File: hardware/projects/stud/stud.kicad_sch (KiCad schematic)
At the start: 6 parts, among them IC1 R7KA8M2JFLCAC#UC0, IC2 IS42S32160F-7BLI, U1 TPS629210DRLR, U2 TAC5242, Y1 X1G0044510004

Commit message: label other signal lines
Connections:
- net EXTAL: now reaches Y1.3 (OUT)
- net EXTAL: now also IC1.K17 (P212/E_XTAL)
- net μSD_DAT2: now reaches MICRO_SD1.1 (DAT2)
- net μSD_DAT2: now also IC1.B16 (PD01)
- net μSD_DAT3: now reaches MICRO_SD1.2 (CD/DAT3)
- net μSD_DAT3: now also IC1.E8 (P111)
- net μSD_CMD: now reaches MICRO_SD1.3 (CMD)
- net μSD_CMD: now also IC1.C14 (PD04)
- net μSD_CLK: now reaches MICRO_SD1.5 (CLK)
- net μSD_CLK: now also IC1.C16 (PD05)
- net μSD_DAT0: now reaches MICRO_SD1.7 (DAT0)
- net μSD_DAT0: now also IC1.C15 (PD03)
- net μSD_DAT1: now reaches MICRO_SD1.8 (DAT1)
- net μSD_DAT1: now also IC1.B17 (PD02)
- net μSD_CD: now reaches MICRO_SD1.CD1 (CD)
- net μSD_CD: now also IC1.D11 (P306)
- net SSI_RX: now reaches IC1.F14 (P406)
- net SSI_RX: now also U2.4 (DOUT)
- net SSI_TX: now reaches IC1.G12 (P405)
- net SSI_TX: now also U2.5 (DIN)
- net SSI_BCK: now reaches IC1.H13 (P403)
- net SSI_BCK: now also U2.2 (BCLK)
- net SSI_FS: now reaches IC1.J13 (P404)
- net SSI_FS: now also U2.3 (FSYNC)
- no-connect marks 0 -> 6
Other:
- note added: "GPO latched high ⇒ clock error; have to power-cycle to clear, but good debug item?"
- note added: "MICBIAS is an output to bias mics; bring out to test point?"
- note added: "pin groups: - SSI*0_A for audio - SD0*_C for μSD"
- moved on the sheet: Y1

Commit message: hook up all chips except the 3.3 V buck
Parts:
- added C1, C10, C11, C12, C13, C14, C15, C17, C2, C3, C31, C32, C33, C34, C35, C36, C37, C38, C39, C4, C40, C41, C42, C43, C44, C45, C48, C5, C50, C52, C6, C7, C8, C9: 100n, symbol Device:C
- added C16, C46, C47, C49, C53, C54, C55: 22u, symbol Device:C
- added C18, C19, C20, C21, C22, C23, C24, C25, C26, C27, C28, C29: 220n, symbol Device:C
- added C30: 47u, symbol Device:C
- added C51: 1u, symbol Device:C
- added C58, C59: 2.2u, symbol Device:C
- added JP1: SolderJumper_2_Bridged, symbol Jumper:SolderJumper_2_Bridged
- added L1: 2.2u, symbol Device:L
- added R1: 5.1, symbol Device:R_US
- added R2, R3: 100k, symbol Device:R_US
- added TP1, TP2: TestPoint, symbol Connector:TestPoint
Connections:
- net SHIELD is gone; now on net GND: MICRO_SD1.MP2 (SHIELD), MICRO_SD1.MP3 (SHIELD), MICRO_SD1.MP4 (SHIELD)
- net +3V3: now reaches Y1.1 (~{ST})
- net +3V3: now also IC1.A10 (VCC_DCDC_1), IC1.A11 (VCC_DCDC_2), IC1.B10 (VCC_DCDC_3), IC1.B11 (VCC_DCDC_4), IC1.F11 (VCC_07), IC1.F6 (VCC_08), IC1.G11 (VCC_06), IC1.G16 (VCC_05), IC1.G6 (VCC_09), IC1.H11 (VCC_04), IC1.H14 (VCC_03), IC1.H6 (VCC_10), IC1.J6 (VCC2_11), IC1.K14 (VCC_02), IC1.L15 (VCC_01), IC1.L6 (VCC2_12), IC1.M7 (VCC2_14), IC1.M8 (VCC2_15), IC1.R1 (VCC2_13), IC2.A7 (VDD_1), IC2.B2 (VDDQ_1), IC2.B7 (VDDQ_2), IC2.C9 (VDDQ_3), IC2.D9 (VDDQ_4), IC2.E1 (VDDQ_5), IC2.F9 (VDD_2), IC2.L1 (VDDQ_6), IC2.L7 (VDD_3), IC2.M9 (VDDQ_7), IC2.N9 (VDDQ_8), IC2.P2 (VDDQ_9), IC2.P7 (VDDQ_10), IC2.R7 (VDD_4), MICRO_SD1.4 (VDD), U2.12 (MD5), U2.6 (IOVDD), Y1.4 (VCC), C1.1, C10.1, C11.1, C12.1, C13.1, C14.1, C15.1, C16.1, C17.1, C2.1, C3.1, C31.1, C32.1, C33.1, C34.1, C35.1, C36.1, C37.1, C38.1, C39.1, C4.1, C40.1, C41.1, C42.1, C43.1, C44.1, C45.2, C5.1, C52.1, C6.1, C7.1, C8.1, C9.1, R1.1
- net GND: now reaches Y1.2 (GND)
- net GND: now also IC1.A9 (VSS_DCDC_1), IC1.B9 (VSS_DCDC_2), IC1.F10 (VSS_07), IC1.F7 (VSS_08), IC1.F8 (VSS3), IC1.G10 (VSS_06), IC1.G15 (VSS_03), IC1.G17 (VSS_05), IC1.G7 (VSS_09), IC1.G8 (VSS4), IC1.H10 (VSS5), IC1.H7 (VSS_10), IC1.H8 (VSS7), IC1.J10 (VSS6), IC1.J12 (VSS2), IC1.J14 (VSS_02), IC1.J7 (VSS_11), IC1.K10 (VSS8), IC1.K12 (VSS1), IC1.K6 (VSS_12), IC1.K7 (VSS9), IC1.L12 (VSS0), IC1.L7 (VSS_14), IC1.L8 (VSS_15), IC1.L9 (VSS10), IC1.M10 (VSS11), IC1.M17 (VSS_01), IC1.U4 (VSS_13), IC2.A3 (VSS_1), IC2.B3 (VSSQ_1), IC2.B8 (VSSQ_2), IC2.C1 (VSSQ_3), IC2.D1 (VSSQ_4), IC2.E9 (VSSQ_5), IC2.F1 (VSS_2), IC2.L3 (VSS_3), IC2.L9 (VSSQ_6), IC2.M1 (VSSQ_7), IC2.N1 (VSSQ_8), IC2.P3 (VSSQ_9), IC2.P8 (VSSQ_10), IC2.R3 (VSS_4), MICRO_SD1.6 (VSS), MICRO_SD1.MP1 (SHIELD), U2.10 (MD4), U2.13 (MD0), U2.7 (MD1), U2.8 (MD2), U2.9 (MD3), C1.2, C10.2, C11.2, C12.2, C13.2, C14.2, C15.2, C16.2, C17.2, C18.2, C19.2, C2.2, C20.2, C21.2, C22.2, C23.2, C24.2, C25.2, C26.2, C27.2, C28.2, C29.2, C3.2, C30.2, C31.2, C32.2, C33.2, C34.2, C35.2, C36.2, C37.2, C38.2, C39.2, C4.2, C40.2, C41.2, C42.2, C43.2, C44.2, C45.1, C49.2, C5.2, C50.2, C52.2, C6.2, C7.2, C8.2, C9.2, JP1.2 (B)
- net VLO: now reaches IC1.A7 (VLO_1)
- net VLO: now also IC1.A8 (VLO_2), IC1.B7 (VLO_3), IC1.B8 (VLO_4), L1.1
- net +0V9: now reaches IC1.G9 (VCL4)
- net +0V9: now also IC1.H9 (VCL5), IC1.J8 (VCL7), IC1.J9 (VCL6), IC1.K11 (VCL1), IC1.K8 (VCL9), IC1.K9 (VCL8), IC1.L11 (VCL0), IC1.M11 (VCL11), C18.1, C19.1, C20.1, C21.1, C22.1, C23.1, C24.1, C25.1, C26.1, C27.1, C28.1, C29.1, C30.1, L1.2
- net at U2.1 (DREG): now also C49.1, C50.1
- net CODEC_ERROR: now reaches U2.11 (GPO)
- net CODEC_ERROR: now also TP2.1
- net at U2.14 (MICBIAS): now also TP1.1
- net at U2.15 (IN1P): now also C47.2
- net at U2.16 (IN1M): now also C53.2
- net at U2.17 (IN2P): now also C54.2
- net at U2.18 (IN2M): now also C55.2
- net at U2.20 (OUT1P): now also C58.1
- net at U2.21 (OUT2P): now also C59.1
- net +3V3A: now reaches U2.23 (AVDD)
- net +3V3A: now also C46.1, C48.1, R1.2
- net at U2.24 (VREF): now also C51.1
- net GNDA: now reaches U2.A1 (VSS)
- net GNDA: now also U2.A2 (VSS), U2.A3 (VSS), U2.A4 (VSS), U2.TP (VSS), C46.2, C48.2, C51.2, C53.1, C55.1, JP1.1 (A), R2.2, R3.2
- new net IN_L: C47.1
- new net IN_R: C54.1
- new net OUT_L: C58.2, R3.1
- new net OUT_R: C59.2, R2.1
- no-connect marks 6 -> 8
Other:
- note added: "VLO buck output"
- note added: "bypass caps for VCC_01 to VCC2_15"
- note added: "bypass caps for VCC_DCDC"
- note added: "bypass caps for VCL0 to VLC11"
- note added: "bypass caps for VDD/VDDQ"
- note added: "configured for - target I2S - AVDD = 3V3, 32-bit word, linear-phase - input HPF cutoff @ 1 Hz - single-ended I/O, AC-coupled"
- moved on the sheet: IC2, MICRO_SD1, U1, U2, Y1

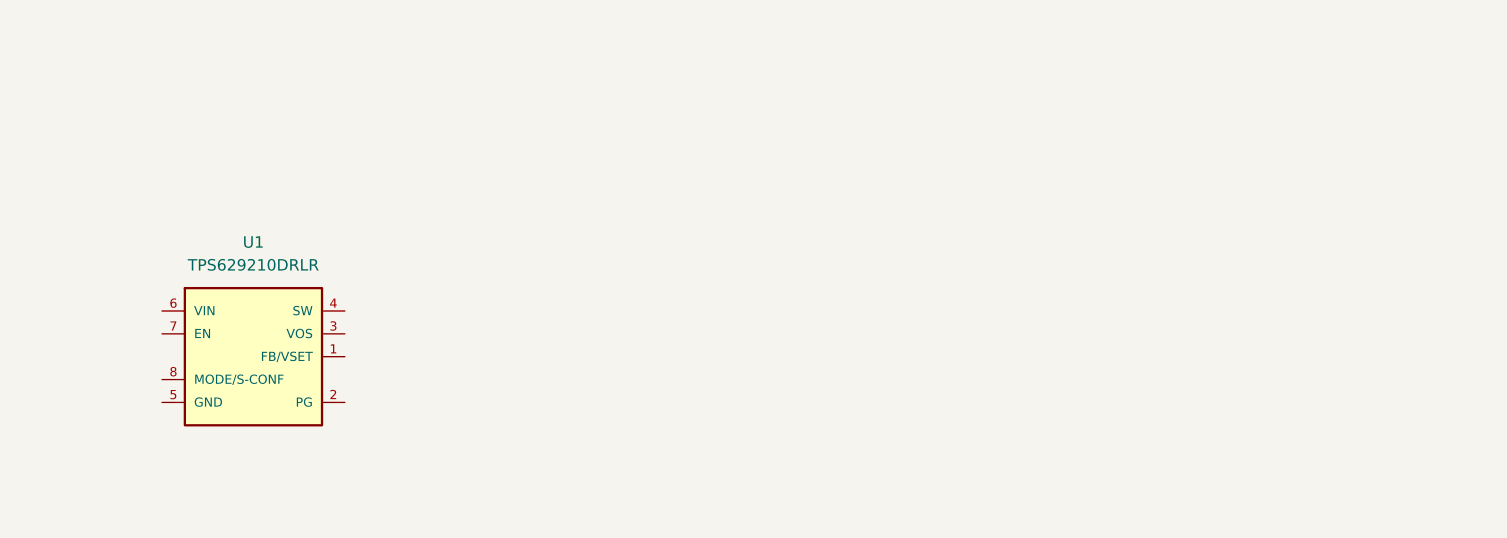
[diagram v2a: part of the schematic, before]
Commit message: set up buck converter
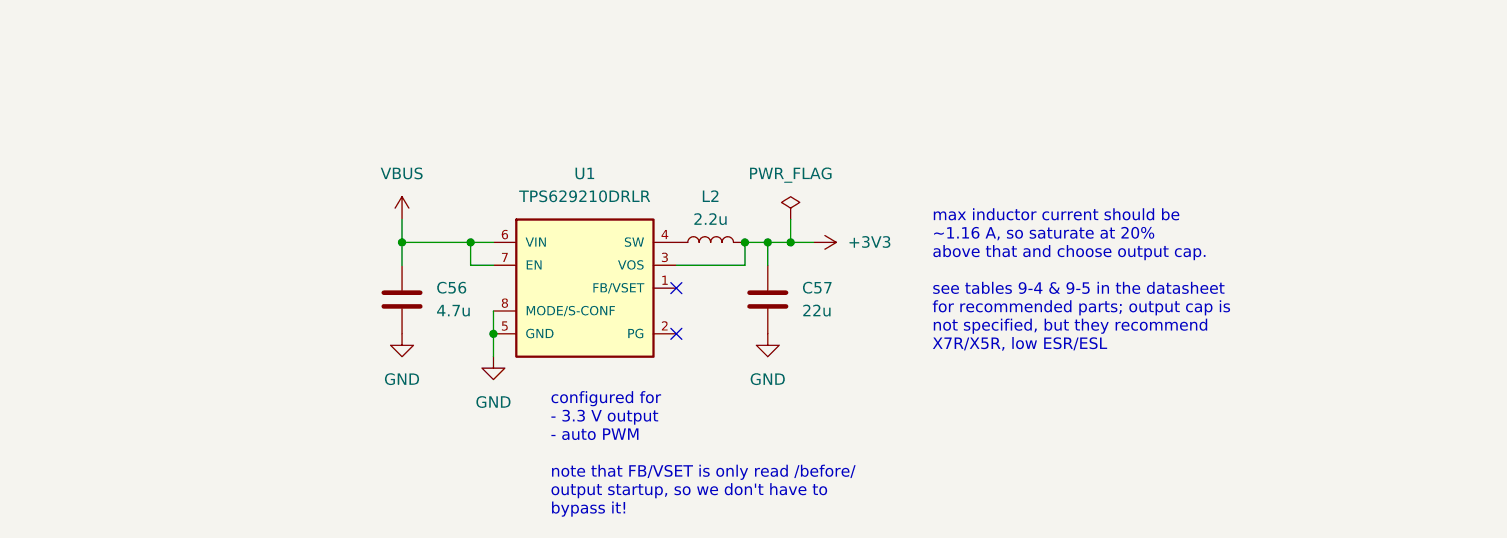
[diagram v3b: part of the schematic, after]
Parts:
- added C56: 4.7u, symbol Device:C
- added C57: 22u, symbol Device:C
- added L2: 2.2u, symbol Device:L
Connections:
- net +3V3: now also U1.3 (VOS), C57.1, L2.2
- net GND: now also U1.5 (GND), U1.8 (MODE/S-CONF), C56.2, C57.2
- net at U1.4 (SW): now also L2.1
- net VBUS: now reaches U1.6 (VIN)
- net VBUS: now also U1.7 (EN), C56.1
- no-connect marks 8 -> 10
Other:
- note added: "configured for - 3.3 V output - auto PWM note that FB/VSET is only read /before/ output startup, so we don't have to bypass it!"
- note added: "max inductor current should be ~1.16 A, so saturate at 20% above that and choose output cap. see tables 9-4 & 9-5 in the datasheet for recommended parts; output cap is not specified, but they recommend X7R/X5R, low ESR/ESL"
- moved on the sheet: U1

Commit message: add a USB port
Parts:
- added D1, D2: D, symbol Device:D
- added J1: USB_C_Receptacle_USB2.0_16P, Connector_USB:USB_C_Receptacle_G-Switch_GT-USB-7010ASV, symbol Connector:USB_C_Receptacle_USB2.0_16P
- added R4: 2.20k 1%, symbol Device:R_US
- added R5, R6: 5.1k, symbol Device:R_US
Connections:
- net +3V3: now also IC1.H15 (VCC_USBHS), IC1.K15 (AVCC_USBHS), IC1.U17 (VCC_USB)
- net GND: now also IC1.H12 (VSS_04), IC1.J16 (VSS2_USBHS), IC1.J17 (VSS1_USBHS), IC1.T17 (VSS_USB), J1.A1 (GND), J1.A12 (GND), J1.B1 (GND), J1.B12 (GND), J1.SH (SHIELD), R4.2, R5.2, R6.2
- net VBUS: now also IC1.M15 (P408), D1.2 (A), J1.A4 (VBUS), J1.A9 (VBUS), J1.B4 (VBUS), J1.B9 (VBUS); no longer C56.1, U1.6 (VIN), U1.7 (EN)
- net USB_D+: now reaches IC1.H16 (USBHS_DP)
- net USB_D+: now also J1.A6 (D+), J1.B6 (D+)
- net USB_D-: now reaches IC1.H17 (USBHS_DM)
- net USB_D-: now also J1.A7 (D-), J1.B7 (D-)
- net at IC1.J15 (USBHS_RREF): now also R4.1
- new net: J1.B5 (CC2), R6.1
- new net: J1.A5 (CC1), R5.1
- new net +9V: D2.2 (A)
- new net VDC: C56.1, D1.1 (K), D2.1 (K), U1.6 (VIN), U1.7 (EN)
- no-connect marks 10 -> 12

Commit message: decide on a few IO pins
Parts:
- added J2: DAC0, custom:Connector_01x01_CastellatedEdge, symbol custom:Connector_01x01_CastellatedEdge
- added J3: ADC1_8, custom:Connector_01x01_CastellatedEdge, symbol custom:Connector_01x01_CastellatedEdge
- added J4: DAC1, custom:Connector_01x01_CastellatedEdge, symbol custom:Connector_01x01_CastellatedEdge
- added J5: ADC1_6, custom:Connector_01x01_CastellatedEdge, symbol custom:Connector_01x01_CastellatedEdge
- added J6: ADC1_0, custom:Connector_01x01_CastellatedEdge, symbol custom:Connector_01x01_CastellatedEdge
- added J7: ADC1_2, custom:Connector_01x01_CastellatedEdge, symbol custom:Connector_01x01_CastellatedEdge
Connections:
- net at IC1.T8 (P014): now also J2.1
- net at IC1.U11 (P008): now also J3.1
- net at IC1.U12 (P006): now also J5.1
- net at IC1.U13 (P000): now also J6.1
- net at IC1.U14 (P002): now also J7.1
- net at IC1.U8 (P015): now also J4.1

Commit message: choose two I2C interfaces
that might be too many, given that there's a more configurable
peripheral interface. maybe only one hardware I2C and the rest are
"simple?"
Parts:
- added J10: SCL1_A, custom:Connector_01x01_CastellatedEdge, symbol custom:Connector_01x01_CastellatedEdge
- added J11: SDA1_A, custom:Connector_01x01_CastellatedEdge, symbol custom:Connector_01x01_CastellatedEdge
- added J8: SCL0_A, custom:Connector_01x01_CastellatedEdge, symbol custom:Connector_01x01_CastellatedEdge
- added J9: SDA0_A, custom:Connector_01x01_CastellatedEdge, symbol custom:Connector_01x01_CastellatedEdge
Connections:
- net at IC1.K13 (P410): now also J8.1
- net at IC1.P13 (P512): now also J10.1
- net at IC1.R16 (P409): now also J9.1
- net at IC1.U15 (P511): now also J11.1

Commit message: talk to claude about SDRAM and GPIOs
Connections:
- net +0V9: now also IC1.F9 (VCL3), IC1.J11 (VCL2), IC1.L10 (VCL10)
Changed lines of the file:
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@@
 	)
 	(symbol
+		(lib_id "custom:+0V9")
+		(at 107.95 180.34 270)
+		(unit 1)
+		(body_style 1)
+		(exclude_from_sim no)
+		(in_bom yes)
+		(on_board yes)
+		(in_pos_files yes)
+		(dnp no)
+		(fields_autoplaced yes)
+		(property "Reference" "#PWR0140"
+			(at 104.14 180.34 0)
+			(hide yes)
+			(show_name no)
+			(do_not_autoplace no)
+			(effects
+				(font
+					(size 1.27 1.27)
+				)
+			)
+		)
+		(property "Value" "+0V9"
+			(at 111.76 180.3399 90)
+			(show_name no)
+			(do_not_autoplace no)
+			(effects
+				(font
+					(size 1.27 1.27)
+				)
+				(justify left)
+			)
+		)
+		(property "Footprint" ""
+			(at 107.95 180.34 0)
+			(hide yes)
+			(show_name no)
+			(do_not_autoplace no)
+			(effects
+				(font
+					(size 1.27 1.27)
+				)
+			)
+		)
+		(property "Datasheet" ""
+			(at 107.95 180.34 0)
+			(hide yes)
+			(show_name no)
+			(do_not_autoplace no)
+			(effects
+				(font
+					(size 1.27 1.27)
+				)
+			)
+		)
+		(property "Description" "Power symbol creates a global label with name \"+0V9\""
+			(at 107.95 180.34 0)
+			(hide yes)
+			(show_name no)
+			(do_not_autoplace no)
+			(effects
+				(font
+					(size 1.27 1.27)
+				)
+			)
+		)
+		(pin "1"
+		)
+		(instances
+			(project "stud"
+				(path "/5a440a9e-b660-4605-bd2b-6a991cc5b149"
+					(reference "#PWR0140")
+					(unit 1)
+				)
+			)
+		)
+	)
+	(symbol
 		(lib_id "Device:R_US")
 		(at 326.39 402.59 0)
@@
 	)
 	(symbol
+		(lib_id "custom:+0V9")
+		(at 46.99 330.2 90)
+		(unit 1)
+		(body_style 1)
+		(exclude_from_sim no)
+		(in_bom yes)
+		(on_board yes)
+		(in_pos_files yes)
+		(dnp no)
+		(fields_autoplaced yes)
+		(property "Reference" "#PWR0139"
+			(at 50.8 330.2 0)
+			(hide yes)
+			(show_name no)
+			(do_not_autoplace no)
+			(effects
+				(font
+					(size 1.27 1.27)
+				)
+			)
+		)
+		(property "Value" "+0V9"
+			(at 43.18 330.1999 90)
+			(show_name no)
+			(do_not_autoplace no)
+			(effects
+				(font
+					(size 1.27 1.27)
+				)
+				(justify left)
+			)
+		)
+		(property "Footprint" ""
+			(at 46.99 330.2 0)
+			(hide yes)
+			(show_name no)
+			(do_not_autoplace no)
+			(effects
+				(font
+					(size 1.27 1.27)
+				)
+			)
+		)
+		(property "Datasheet" ""
+			(at 46.99 330.2 0)
+			(hide yes)
+			(show_name no)
+			(do_not_autoplace no)
+			(effects
+				(font
+					(size 1.27 1.27)
+				)
+			)
+		)
+		(property "Description" "Power symbol creates a global label with name \"+0V9\""
+			(at 46.99 330.2 0)
+			(hide yes)
+			(show_name no)
+			(do_not_autoplace no)
+			(effects
+				(font
+					(size 1.27 1.27)
+				)
+			)
+		)
+		(pin "1"
+		)
+		(instances
+			(project "stud"
+				(path "/5a440a9e-b660-4605-bd2b-6a991cc5b149"
+					(reference "#PWR0139")
+					(unit 1)
+				)
+			)
+		)
+	)
+	(symbol
 		(lib_id "power:GND")
 		(at 107.95 241.3 90)
@@
 					(unit 1)
 				)
+			)
+		)
+	)
+	(symbol
+		(lib_id "custom:+0V9")
+		(at 107.95 96.52 270)
+		(unit 1)
+		(body_style 1)
+		(exclude_from_sim no)
+		(in_bom yes)
+		(on_board yes)
+		(in_pos_files yes)
+		(dnp no)
+		(fields_autoplaced yes)
+		(property "Reference" "#PWR0138"
+			(at 104.14 96.52 0)
+			(hide yes)
+			(show_name no)
+			(do_not_autoplace no)
+			(effects
+				(font
+					(size 1.27 1.27)
+				)
+			)
+		)
+		(property "Value" "+0V9"
+			(at 111.76 96.5199 90)
+			(show_name no)
+			(do_not_autoplace no)
+			(effects
+				(font
+					(size 1.27 1.27)
+				)
+				(justify left)
+			)
+		)
+		(property "Footprint" ""
+			(at 107.95 96.52 0)
+			(hide yes)
+			(show_name no)
+			(do_not_autoplace no)
+			(effects
+				(font
+					(size 1.27 1.27)
+				)
+			)
+		)
+		(property "Datasheet" ""
+			(at 107.95 96.52 0)
+			(hide yes)
+			(show_name no)
+			(do_not_autoplace no)
+			(effects
+				(font
+					(size 1.27 1.27)
+				)
+			)
+		)
+		(property "Description" "Power symbol creates a global label with name \"+0V9\""
+			(at 107.95 96.52 0)
+			(hide yes)
+			(show_name no)
+			(do_not_autoplace no)
+			(effects
+				(font
+					(size 1.27 1.27)
+				)
+			)
+		)
+		(pin "1"
+		)
+		(instances
+			(project "stud"
+				(path "/5a440a9e-b660-4605-bd2b-6a991cc5b149"
+					(reference "#PWR0138")
+					(unit 1)
+				)
